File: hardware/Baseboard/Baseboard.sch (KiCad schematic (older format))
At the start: 0 parts

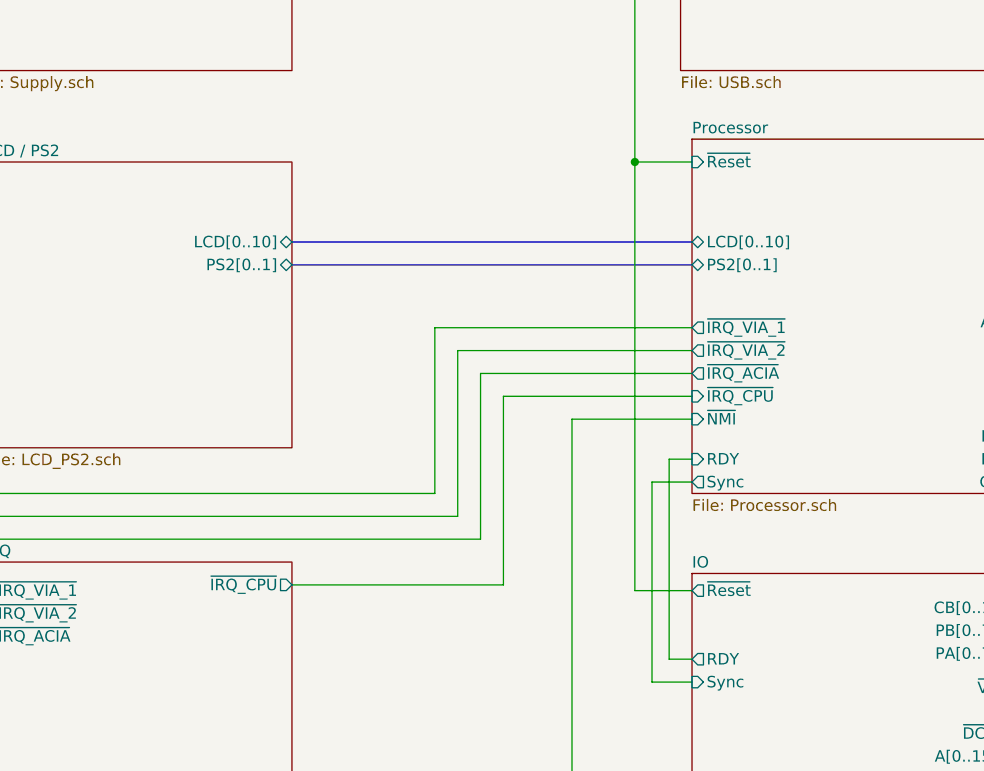
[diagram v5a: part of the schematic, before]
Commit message: Add pull up resistors for PS/2, add LCD backlight switch
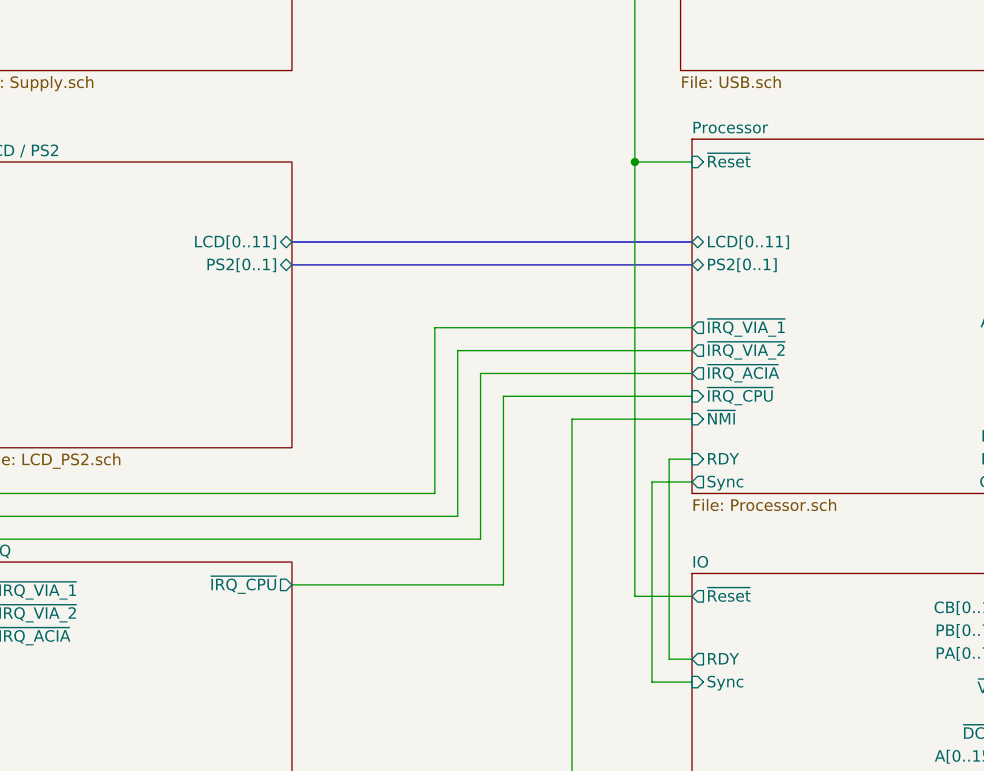
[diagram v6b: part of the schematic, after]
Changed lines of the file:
@@
 F5 "R~W" I R 9650 9150 50
 F6 "Clock" I R 9650 9250 50
-F7 "~Reset" O L 8250 8225 50
+F7 "~Reset" O L 8250 8250 50
 F8 "CB[0..1]" O R 9650 8300 50
 F9 "A[0..15]" I R 9650 8950 50
@@
 F0 "LCD / PS2" 50
 F1 "LCD_PS2.sch" 50
-F2 "LCD[0..10]" B R 6500 6700 50
-F3 "PS2[0..1]" B R 6500 6800 50
+F2 "PS2[0..1]" B R 6500 6800 50
+F3 "LCD[0..11]" B R 6500 6700 50
 $EndSheet
 $Sheet
@@
 F6 "~NMI" I L 8250 7475 50
 F7 "R~W" O R 9850 7250 50
-F8 "LCD[0..10]" B L 8250 6700 50
-F9 "PS2[0..1]" B L 8250 6800 50
-F10 "Clock" O R 9850 7350 50
-F11 "~Reset" I L 8250 6350 50
-F12 "~IRQ_VIA_2" O L 8250 7175 50
-F13 "~IRQ_VIA_1" O L 8250 7075 50
-F14 "~IRQ_ACIA" O L 8250 7275 50
-F15 "~IRQ_CPU" I L 8250 7375 50
-F16 "CB[0..1]" I R 9850 7750 50
-F17 "A[0..15]" O R 9850 7050 50
-F18 "D[0..7]" B R 9850 7150 50
-F19 "RDY" I L 8250 7650 50
-F20 "Sync" O L 8250 7750 50
-F21 "~VP" O R 9850 7450 50
-F22 "~RTS" O R 9850 6550 50
-F23 "~CTS" I R 9850 6650 50
-F24 "~DSR" I R 9850 6850 50
-F25 "~DTR" O R 9850 6750 50
-F26 "~DCD" I R 9850 6950 50
+F8 "PS2[0..1]" B L 8250 6800 50
+F9 "Clock" O R 9850 7350 50
+F10 "~Reset" I L 8250 6350 50
+F11 "~IRQ_VIA_2" O L 8250 7175 50
+F12 "~IRQ_VIA_1" O L 8250 7075 50
+F13 "~IRQ_ACIA" O L 8250 7275 50
+F14 "~IRQ_CPU" I L 8250 7375 50
+F15 "CB[0..1]" I R 9850 7750 50
+F16 "A[0..15]" O R 9850 7050 50
+F17 "D[0..7]" B R 9850 7150 50
+F18 "RDY" I L 8250 7650 50
+F19 "Sync" O L 8250 7750 50
+F20 "~VP" O R 9850 7450 50
+F21 "~RTS" O R 9850 6550 50
+F22 "~CTS" I R 9850 6650 50
+F23 "~DSR" I R 9850 6850 50
+F24 "~DTR" O R 9850 6750 50
+F25 "~DCD" I R 9850 6950 50
+F26 "LCD[0..11]" B L 8250 6700 50
 $EndSheet
 Wire Bus Line
@@
 	8150 8525 8250 8525
 Wire Wire Line
-	8250 8225 8000 8225
-Wire Wire Line
 	8250 6350 8000 6350
 Connection ~ 8000 6350
-Wire Wire Line
-	8000 6350 8000 8225
 Wire Wire Line
 	6500 4800 8000 4800
@@
 Wire Wire Line
 	6500 4900 8200 4900
+Wire Wire Line
+	8250 8250 8000 8250
+Wire Wire Line
+	8000 6350 8000 8250
 $EndSCHEMATC
